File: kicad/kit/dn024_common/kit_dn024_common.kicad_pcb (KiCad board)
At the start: 2 copper layers, 55 x 90 mm, 5 parts, among them J1 SMA edge launch

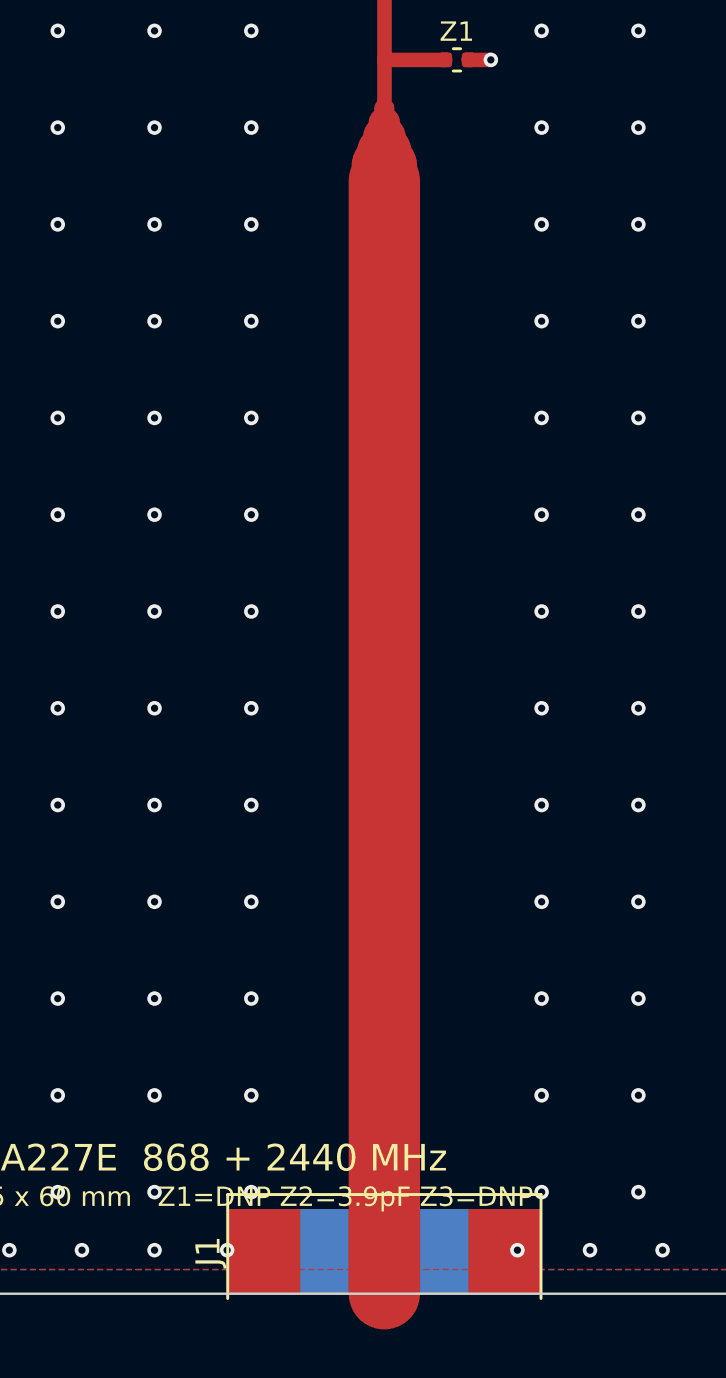
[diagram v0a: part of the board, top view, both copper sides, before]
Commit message: Kit launches through U.FL and a pigtail, not an SMA on the board edge
Embever's own antenna kit feeds its boards through a U.FL and a pigtail
to a bulkhead SMA. That is the better arrangement for a measurement kit
and the kit now does it.

The connector is the smaller half of the reason. The real one is that on
a 45 x 60 mm plane at 868 MHz - lambda 345 mm - the plane and whatever
cable leaves it are one conductor as far as common-mode current goes, so
the braid is part of the antenna and the S11 null moves when the cable
moves. Nothing about the connector fixes that. What U.FL does is let you
fix it: the bulkhead SMA stays on the jig instead of leaving a connector
shell and its ground tabs as copper beside a plane that is half the
antenna, and the pigtail is somewhere to put a ferrite or a sleeve balun,
which is the only real cure. The checklist and the measurement procedure
now both start with choking the cable and proving it by moving it.

The land pattern is Hirose's own for the U.FL-R-SMT-1(10) - signal pad
1.05 x 1.00, ground pads 2.20 x 1.05 - taken from KiCad's
Connector_Coaxial library, which cites Hirose's page for the part. It is
regenerated from those dimensions rather than copied, so the provenance
sits next to the geometry; KiCad's libraries are CC-BY-SA 4.0 with a
design exception and this is the attribution.

A 1.05 mm pad will not take a 2.95 mm line, the same trap the through-
hole SMA sprang with its ground posts. The line tapers 2.95 -> 1.0 mm
over 2.5 mm and runs 1.5 mm into the pad, and the pour keep-away now
stops above the connector so the pour closes around J1's ground pads.
That turns the neck into a grounded coplanar line instead of a
microstrip: line_impedance.py puts 1.0 mm with a 0.2 mm gap at 53.9 ohm
against 84.5 ohm bare, so the neck is near 50 ohm by construction rather
than a lump for the network to absorb.

The launch needed its own rules, because the general ones do not cover
it: a track and the pad it runs to are the same net, s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
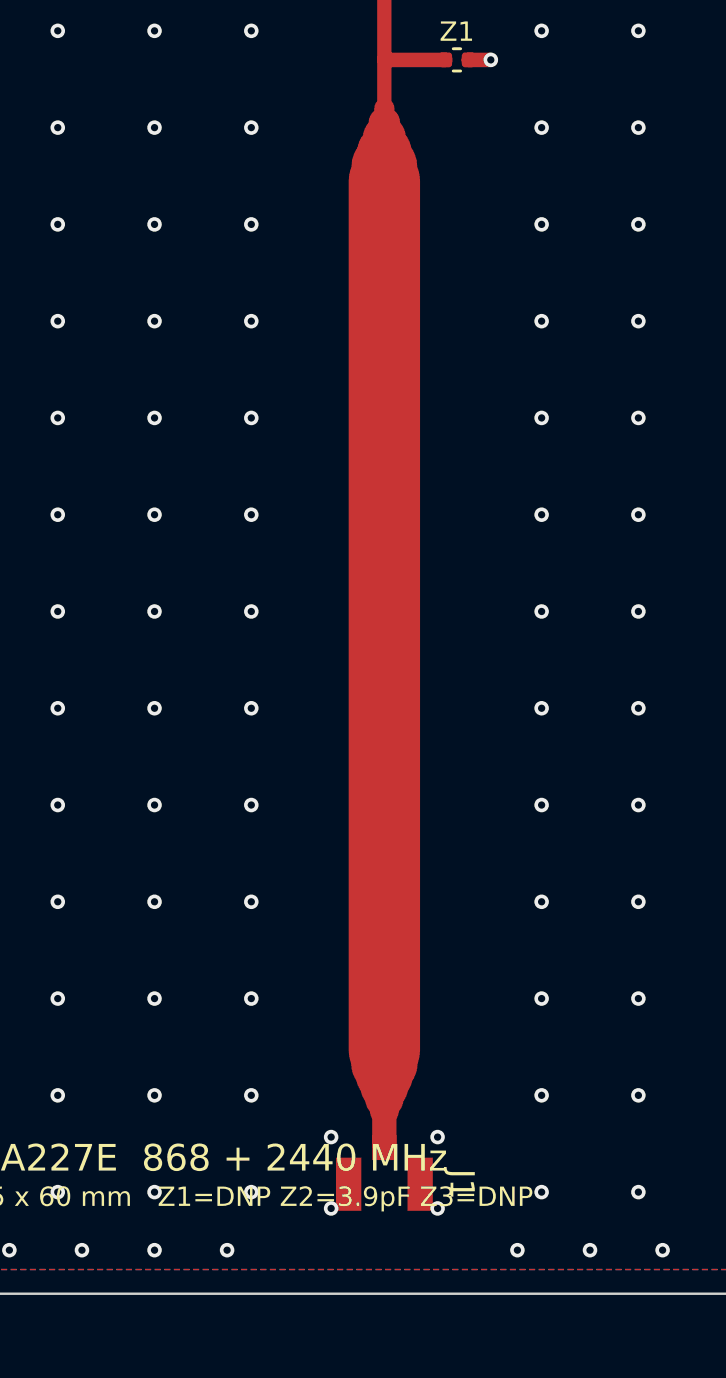
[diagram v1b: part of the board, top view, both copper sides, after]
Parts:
- J1: value SMA edge launch -> U.FL receptacle; footprint SWRA117D_RF:SMA_EdgeMount_Generic -> SWRA117D_RF:U_FL_Hirose_U_FL_R_SMT_1_Vertical
- moved J1 5.00 mm to (127.5, 145.0), turned to 270 degrees
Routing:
- net RF_IN: track 56.5 -> 50.5 mm
- net GND: vias 151 -> 155
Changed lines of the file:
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@@
 	(net 2 "ANT_FEED")
 	(net 3 "RF_IN")
-	(footprint "SWRA117D_RF:SMA_EdgeMount_Generic"
-		(layer "F.Cu")
-		(at 127.5 150 90)
-		(descr "Generic end-launch (edge-mount) SMA jack, generated for a 1.6 mm substrate (er 4.5). Signal pad 2.95 mm wide to match the 50 ohm line; coplanar ground set back 2.0 mm, which makes the launch 49.8 ohm. Origin sits on the board edge. Pad 1 = signal, pad 2 = shell ground: two tabs on top, one solid plane underneath so the launch keeps its reference without relying on a zone fill."
-		)
-		(tags "SMA edge launch end launch RF connector 50 ohm")
+	(footprint "SWRA117D_RF:U_FL_Hirose_U_FL_R_SMT_1_Vertical"
+		(layer "F.Cu")
+		(at 127.5 145 270)
+		(descr "Hirose U.FL-R-SMT-1(10) vertical coaxial receptacle. Manufacturer's recommended land pattern, via the KiCad Connector_Coaxial library, which cites https://www.hirose.com/product/en/products/U.FL/U.FL-R-SMT-1%2810%29/ . Signal pad 1.05 x 1.0 mm, two ground pads 2.2 x 1.05 mm. The signal pad is 1.0 mm across, so a 50 ohm line on 1.6 mm FR4 (2.95 mm) must taper into it, not butt onto it."
+		)
+		(tags "U.FL IPEX coaxial RF receptacle Hirose 50 ohm")
 		(attr smd)
+		(property "Datasheet" "https://www.hirose.com/product/en/products/U.FL/U.FL-R-SMT-1%2810%29/"
+			(at 0 0 270)
+			(layer "F.Fab")
+			(effects (font (size 1 1)) (hide yes))
+			(unlocked yes)
+		)
 		(property "Reference" "J1"
-			(at 1.75 -7.275 90)
+			(at 0.475 -3.2 270)
 			(layer "F.SilkS")
 			(effects (font (size 1 1) (thickness 0.15)))
 			(unlocked yes)
 		)
-		(property "Value" "SMA edge launch"
-			(at 1.75 7.275 90)
-			(layer "F.Fab")
-			(effects (font (size 1 1) (thickness 0.15)))
-			(unlocked yes)
-		)
-		(fp_text user "%R"
-			(at 1.75 0 90)
+		(property "Value" "U.FL receptacle"
+			(at 0.475 3.2 270)
 			(layer "F.Fab")
 			(effects (font (size 0.8 0.8) (thickness 0.12)))
 			(unlocked yes)
 		)
+		(pad "1" smd rect
+			(at -1.05 0 270)
+			(size 1.05 1)
+			(layers "F.Cu" "F.Paste" "F.Mask")
+			(pinfunction "SIGNAL")
+			(net 3 "RF_IN")
+			(pinfunction "RF_IN")
+			(pintype "passive")
+		)
+		(pad "2" smd rect
+			(at 0.475 1.475 270)
+			(size 2.2 1.05)
+			(layers "F.Cu" "F.Paste" "F.Mask")
+			(pinfunction "GND")
+			(net 1 "GND")
+			(pinfunction "GND")
+			(pintype "passive")
+		)
+		(pad "2" smd rect
+			(at 0.475 -1.475 270)
+			(size 2.2 1.05)
+			(layers "F.Cu" "F.Paste" "F.Mask")
+			(pinfunction "GND")
+			(net 1 "GND")
+			(pinfunction "GND")
+			(pintype "passive")
+		)
 		(fp_line
-			(start -0.2 -6.475)
-			(end 4.1 -6.475)
-			(stroke (width 0.12) (type solid))
-			(layer "F.SilkS")
+			(start -2.02 -2.5)
+			(end 2.28 -2.5)
+			(stroke (width 0.05) (type solid))
+			(layer "F.CrtYd")
 		)
 		(fp_line
-			(start -0.2 6.475)
-			(end 4.1 6.475)
-			(stroke (width 0.12) (type solid))
-			(layer "F.SilkS")
+			(start 2.28 -2.5)
+			(end 2.28 2.5)
+			(stroke (width 0.05) (type solid))
+			(layer "F.CrtYd")
 		)
 		(fp_line
-			(start 4.1 -6.475)
-			(end 4.1 6.475)
-			(stroke (width 0.12) (type solid))
-			(layer "F.SilkS")
+			(start 2.28 2.5)
+			(end -2.02 2.5)
+			(stroke (width 0.05) (type solid))
+			(layer "F.CrtYd")
 		)
 		(fp_line
-			(start -0.2 -6.475)
-			(end 4.1 -6.475)
+			(start -2.02 2.5)
+			(end -2.02 -2.5)
+			(stroke (width 0.05) (type solid))
+			(layer "F.CrtYd")
+		)
+		(fp_line
+			(start -0.425 -1.5)
+			(end 1.775 -1.5)
 			(stroke (width 0.1) (type solid))
 			(layer "F.Fab")
 		)
 		(fp_line
-			(start -0.2 6.475)
-			(end 4.1 6.475)
+			(start 1.775 -1.5)
+			(end 1.775 1.5)
 			(stroke (width 0.1) (type solid))
 			(layer "F.Fab")
 		)
 		(fp_line
-			(start 4.1 -6.475)
-			(end 4.1 6.475)
+			(start 1.775 1.5)
+			(end -0.425 1.5)
 			(stroke (width 0.1) (type solid))
 			(layer "F.Fab")
 		)
-		(fp_rect
-			(start -0.4 -6.675)
-			(end 4.3 6.675)
-			(stroke (width 0.05) (type solid))
-			(fill no)
-			(layer "F.CrtYd")
-		)
-		(fp_rect
-			(start -0.4 -6.675)
-			(end 4.3 6.675)
-			(stroke (width 0.05) (type solid))
-			(fill no)
-			(layer "B.CrtYd")
-		)
-		(pad "1" smd rect
-			(at 1.75 0 90)
-			(size 3.5 2.95)
-			(layers "F.Cu" "F.Paste" "F.Mask")
-			(net 3 "RF_IN")
-			(pinfunction "RF_IN")
-			(pintype "passive")
-		)
-		(pad "2" smd rect
-			(at 1.75 -4.975 90)
-			(size 3.5 3)
-			(layers "F.Cu" "F.Paste" "F.Mask")
-			(net 1 "GND")
-			(pinfunction "GND")
-			(pintype "passive")
-		)
-		(pad "2" smd rect
-			(at 1.75 4.975 90)
-			(size 3.5 3)
-			(layers "F.Cu" "F.Paste" "F.Mask")
-			(net 1 "GND")
-			(pinfunction "GND")
-			(pintype "passive")
-		)
-		(pad "2" smd rect
-			(at 1.75 0 90)
-			(size 3.5 12.95)
-			(layers "B.Cu" "B.Paste" "B.Mask")
-			(net 1 "GND")
-			(pinfunction "GND")
-			(pintype "passive")
+		(fp_line
+			(start -0.425 1.5)
+			(end -0.425 -1.5)
+			(stroke (width 0.1) (type solid))
+			(layer "F.Fab")
 		)
 		(sheetname "Root")
@@
 	(segment
 		(start 127.5 104)
-		(end 127.5 150)
+		(end 127.5 139.95)
 		(width 2.95)
+		(layer "F.Cu")
+		(net 3)
+	)
+	(segment
+		(start 127.5 139.95)
+		(end 127.5 140.45)
+		(width 2.755)
+		(layer "F.Cu")
+		(net 3)
+	)
+	(segment
+		(start 127.5 140.45)
+		(end 127.5 140.95)
+		(width 2.365)
+		(layer "F.Cu")
+		(net 3)
+	)
+	(segment
+		(start 127.5 140.95)
+		(end 127.5 141.45)
+		(width 1.975)
+		(layer "F.Cu")
+		(net 3)
+	)
+	(segment
+		(start 127.5 141.45)
+		(end 127.5 141.95)
+		(width 1.585)
+		(layer "F.Cu")
+		(net 3)
+	)
+	(segment
+		(start 127.5 141.95)
+		(end 127.5 142.45)
+		(width 1.195)
+		(layer "F.Cu")
+		(net 3)
+	)
+	(segment
+		(start 127.5 142.45)
+		(end 127.5 143.95)
+		(width 1)
 		(layer "F.Cu")
 		(net 3)
@@
 	(via
 		(at 131.9 92)
+		(size 0.6)
+		(drill 0.3)
+		(layers "F.Cu" "B.Cu")
+		(net 1)
+	)
+	(via
+		(at 125.3 143.525)
+		(size 0.6)
+		(drill 0.3)
+		(layers "F.Cu" "B.Cu")
+		(net 1)
+	)
+	(via
+		(at 129.7 143.525)
+		(size 0.6)
+		(drill 0.3)
+		(layers "F.Cu" "B.Cu")
+		(net 1)
+	)
+	(via
+		(at 125.3 146.475)
+		(size 0.6)
+		(drill 0.3)
+		(layers "F.Cu" "B.Cu")
+		(net 1)
+	)
+	(via
+		(at 129.7 146.475)
 		(size 0.6)
 		(drill 0.3)
@@
 		)
 		(fill (thermal_gap 0.4) (thermal_bridge_width 0.4))
-		(polygon (pts (xy 124.025 89) (xy 130.975 89) (xy 130.975 150.5) (xy 124.025 150.5)))
+		(polygon (pts (xy 124.025 89) (xy 130.975 89) (xy 130.975 139.95) (xy 124.025 139.95)))
 	)
 	(zone
